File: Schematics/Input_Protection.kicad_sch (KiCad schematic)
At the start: 14 parts, among them J21 43650-0418, J22 464369202, Q6 STB10NK60ZT4

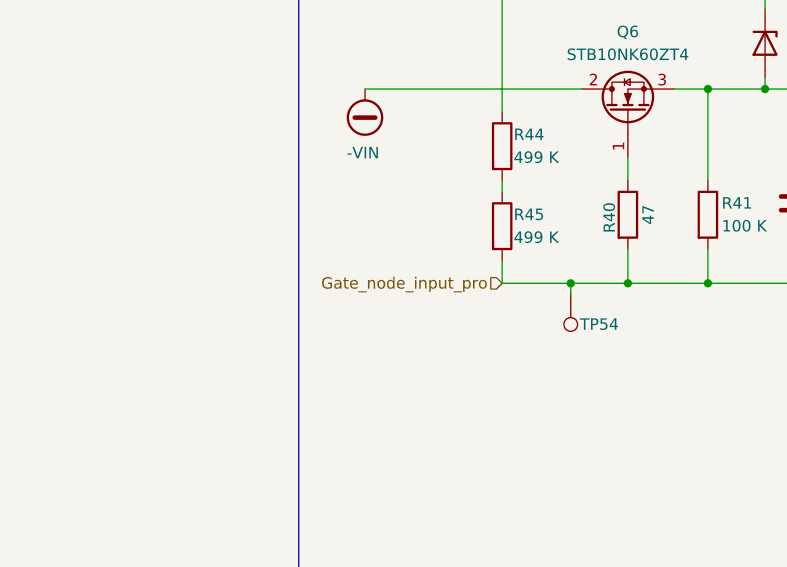
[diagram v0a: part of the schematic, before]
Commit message: Added Precharge Gate Driver to controller and per charge sub circuit
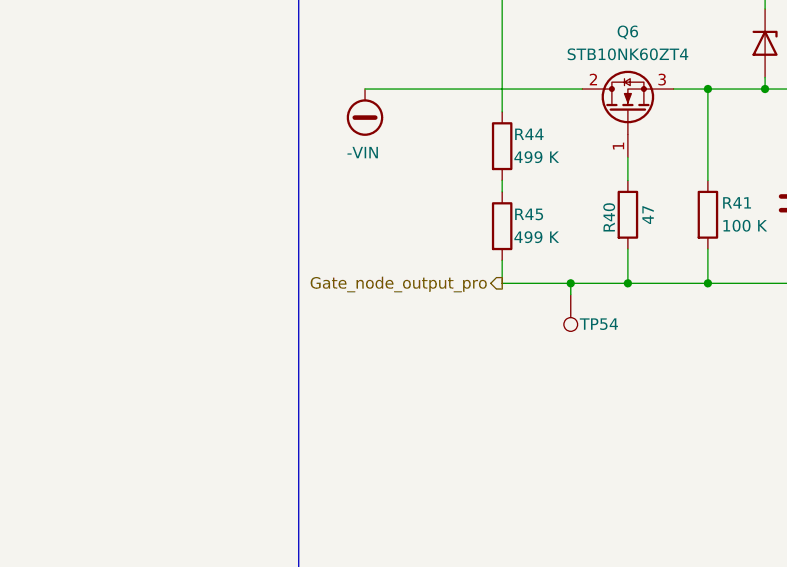
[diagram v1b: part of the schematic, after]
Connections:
- net Gate_node_input_pro: no longer C69.2, D6.1 (K), R40.2, R41.2, R45.2, TP54.1
- new net Gate_node_output_pro: C69.2, D6.1 (K), R40.2, R41.2, R45.2, TP54.1
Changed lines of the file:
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@@
 		)
 	)
-	(hierarchical_label "Gate_node_input_pro"
-		(shape input)
+	(hierarchical_label "Gate_node_output_pro"
+		(shape output)
 		(at 62.23 124.46 180)
 		(effects

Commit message: WIP PCB, Added Test Points, added icon file
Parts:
- renumbered C69 to C66, D5 to D6, D6 to D7, J22 to J23, J21 to J24, Q6 to Q8, R40 to R46, R41 to R47, TP54 to TP67, TP47 to TP68, TP46 to TP69
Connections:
- net Gate_node_input_pro is gone; now on net Gate_node_output_pro: J24.4
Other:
- moved on the sheet: TP67, TP69

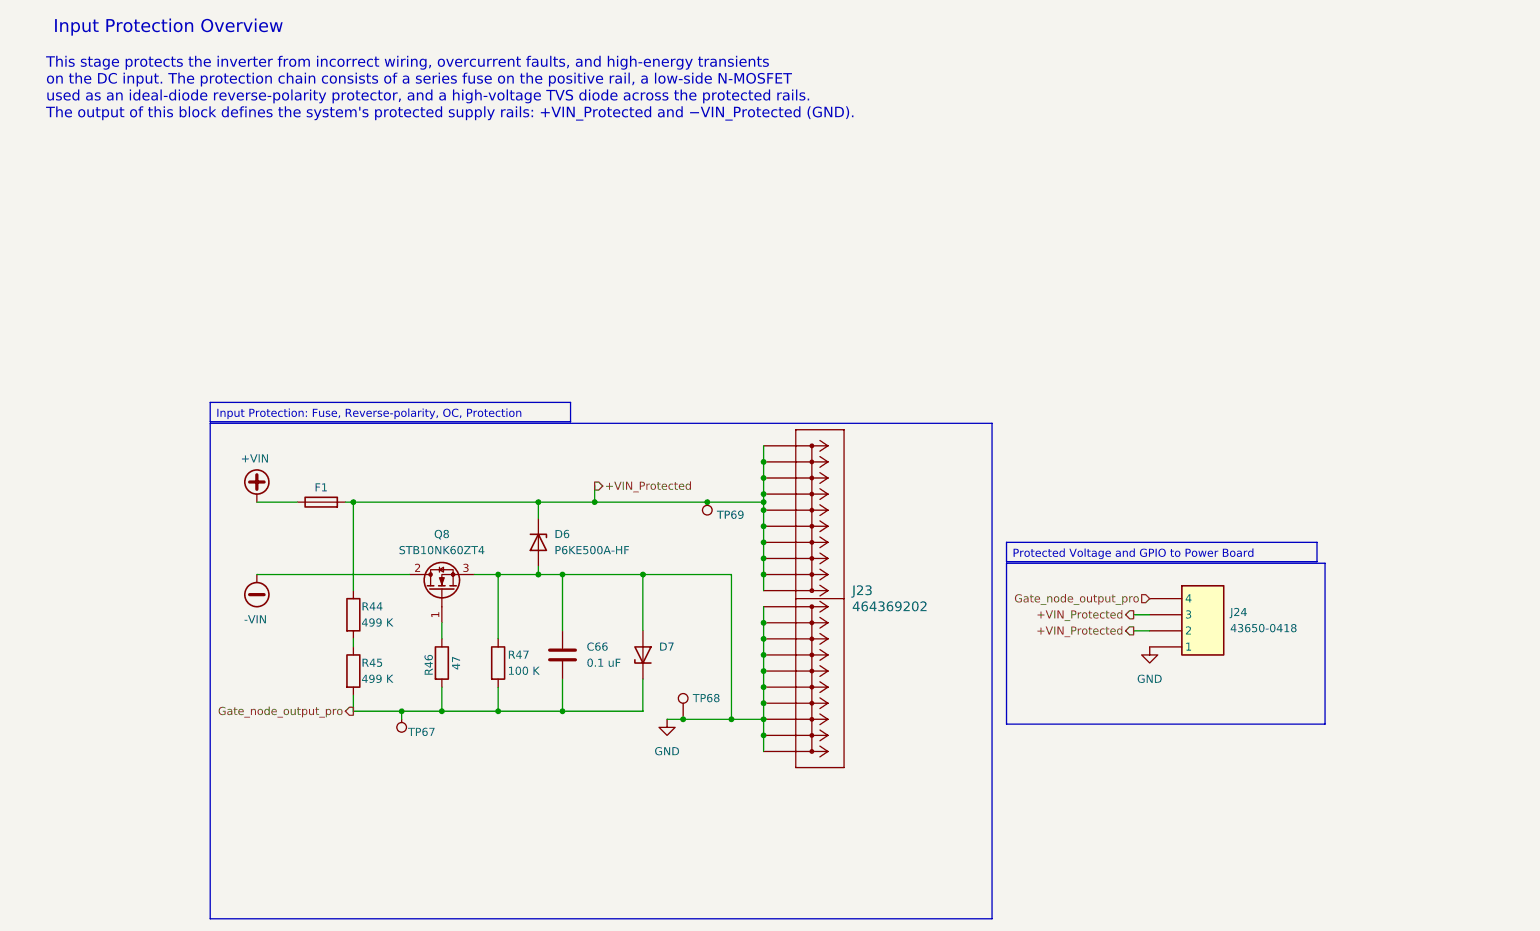
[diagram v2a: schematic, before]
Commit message: WIP PCB Design: Finished DC Input / Protection Circuit
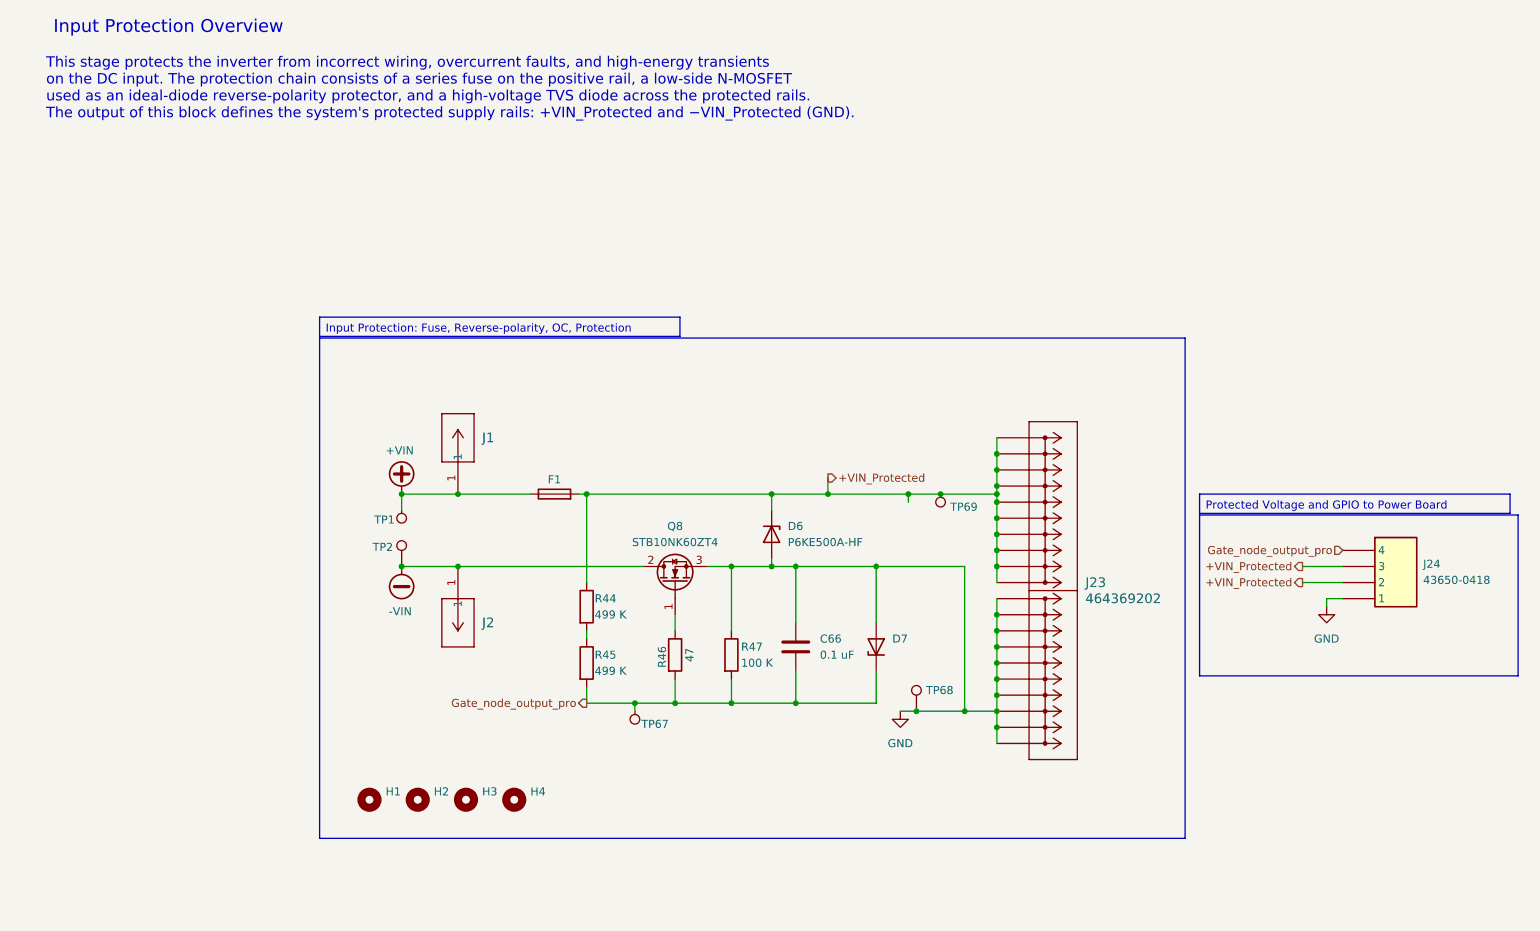
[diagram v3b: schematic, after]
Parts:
- added H1, H2, H3, H4: MountingHole, MountingHole:MountingHole_2.2mm_M2, symbol Mechanical:MountingHole
- added J1: 23AH8786-Red, SiC_Inverter:23AH8786-Red, symbol SiC_Inverter:23AH8786-Red
- added J2: 23AH8785-Black, SiC_Inverter:23AH8785-Black, symbol SiC_Inverter:23AH8785-Black
- added TP1: 5277, SiC_Inverter:5277, symbol SiC_Inverter:5277
- added TP2: 5281, SiC_Inverter:5281, symbol SiC_Inverter:5281
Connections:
- net +VIN: now also J1.1, TP1.1
- net -VIN: now also J2.1, TP2.1
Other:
- moved on the sheet: C66, D6, D7, F1, J23, J24, Q8, R44, R45, R46, R47, TP67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
